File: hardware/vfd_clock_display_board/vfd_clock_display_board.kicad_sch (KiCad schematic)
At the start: 89 parts, among them J1 Conn_01x12_Pin, Q1 2N3906, Q1 MMDT5551, Q11 2N3906, Q12 2N3906, Q13 2N3906, Q14 2N3906, Q15 2N3906, Q16 2N3906, Q18 2N3906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

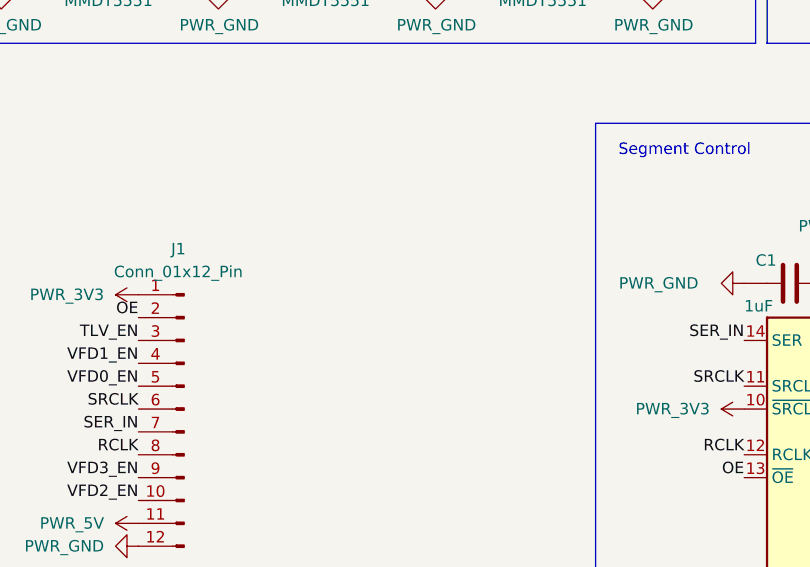
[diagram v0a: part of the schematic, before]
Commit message: Add PCF version of main board, add test pads to display board
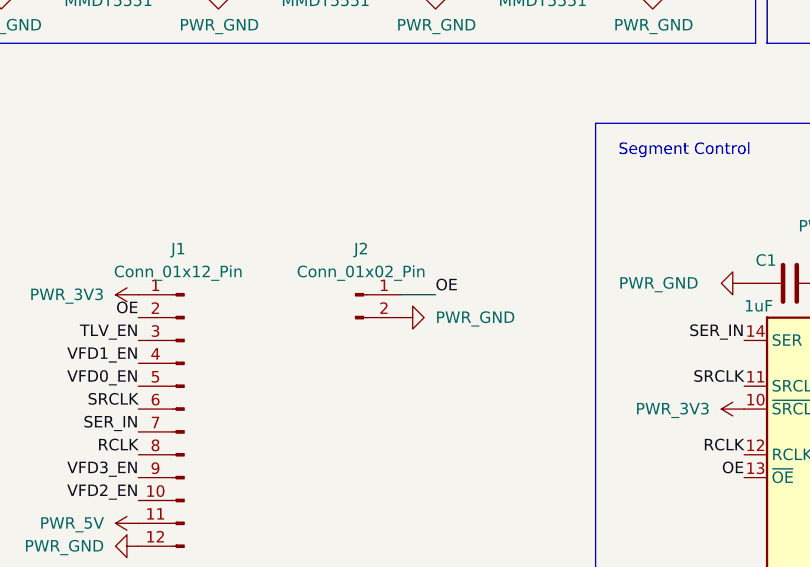
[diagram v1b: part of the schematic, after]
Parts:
- added J2: Conn_01x02_Pin, Connector_PinHeader_2.54mm:PinHeader_1x02_P2.54mm_Vertical, symbol Connector:Conn_01x02_Pin
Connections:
- net OE: now also J2.1 (Pin_1)
- net PWR_GND: now also J2.2 (Pin_2)
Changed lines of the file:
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@@
     (stroke (width 0) (type default))
   )
+  (wire (pts (xy 86.36 147.32) (xy 82.55 147.32))
+    (stroke (width 0) (type default))
+  )
   (wire (pts (xy 110.49 113.03) (xy 110.49 111.76))
     (stroke (width 0) (type default))
@@
     (effects (font (size 1.27 1.27)) (justify right bottom))
   )
-  (label "OE" (at 120.65 167.64 180) (fields_autoplaced)
-    (effects (font (size 1.27 1.27)) (justify right bottom))
-  )
   (label "0QE" (at 161.29 165.1 0) (fields_autoplaced)
     (effects (font (size 1.27 1.27)) (justify left bottom))
@@
     (effects (font (size 1.27 1.27)) (justify right bottom))
   )
+  (label "OE" (at 120.65 167.64 180) (fields_autoplaced)
+    (effects (font (size 1.27 1.27)) (justify right bottom))
+  )
   (label "VFD_C" (at 248.92 36.83 180) (fields_autoplaced)
     (effects (font (size 1.27 1.27)) (justify right bottom))
@@
     (effects (font (size 1.27 1.27)) (justify left bottom))
   )
+  (label "OE" (at 86.36 147.32 0) (fields_autoplaced)
+    (effects (font (size 1.27 1.27)) (justify left bottom))
+  )
   (label "RCLK" (at 120.65 165.1 180) (fields_autoplaced)
     (effects (font (size 1.27 1.27)) (justify right bottom))
@@
     )
   )
+  (symbol (lib_id "Fab:PWR_GND") (at 82.55 149.86 90) (mirror x) (unit 1)
+    (in_bom yes) (on_board yes) (dnp no)
+    (property "Reference" "#PWR013" (at 88.9 149.86 0)
+      (effects (font (size 1.27 1.27)) hide)
+    )
+    (property "Value" "PWR_GND" (at 86.36 149.86 90)
+      (effects (font (size 1.27 1.27)) (justify right))
+    )
+    (property "Footprint" "" (at 82.55 149.86 0)
+      (effects (font (size 1.27 1.27)) hide)
+    )
+    (property "Datasheet" "" (at 82.55 149.86 0)
+      (effects (font (size 1.27 1.27)) hide)
+    )
+    (pin "1")
+    (instances
+      (project "vfd_clock"
+        (path "/3f20cdec-fa58-4248-b6f0-db3d00e652de"
+          (reference "#PWR013") (unit 1)
+        )
+        (path "/3f20cdec-fa58-4248-b6f0-db3d00e652de/d5d05427-319c-448b-a7a3-a42b084031d1"
+          (reference "#PWR09") (unit 1)
+        )
+      )
+      (project "vfd_clock_display_board"
+        (path "/a1603893-10f9-4f34-a9ac-0449eba2410e"
+          (reference "#PWR029") (unit 1)
+        )
+      )
+      (project "vfd_pcb"
+        (path "/cb259c9d-741a-44bb-804a-c4b92b1250f0"
+          (reference "#PWR012") (unit 1)
+        )
+      )
+    )
+  )
   (symbol (lib_id "Transistor_BJT:MMDT5551") (at 100.33 106.68 0) (unit 2)
     (in_bom yes) (on_board yes) (dnp no)
@@
         )
       )
+    )
+  )
+  (symbol (lib_id "Connector:Conn_01x02_Pin") (at 77.47 147.32 0) (unit 1)
+    (in_bom yes) (on_board yes) (dnp no) (fields_autoplaced)
+    (property "Reference" "J2" (at 78.105 142.24 0)
+      (effects (font (size 1.27 1.27)))
+    )
+    (property "Value" "Conn_01x02_Pin" (at 78.105 144.78 0)
+      (effects (font (size 1.27 1.27)))
+    )
+    (property "Footprint" "Connector_PinHeader_2.54mm:PinHeader_1x02_P2.54mm_Vertical" (at 77.47 147.32 0)
+      (effects (font (size 1.27 1.27)) hide)
+    )
+    (property "Datasheet" "~" (at 77.47 147.32 0)
+      (effects (font (size 1.27 1.27)) hide)
+    )
+    (pin "1")
+    (pin "2")
+    (instances
+      (project "vfd_clock_display_board"
+        (path "/a1603893-10f9-4f34-a9ac-0449eba2410e"
+          (reference "J2") (unit 1)
+        )
+      )

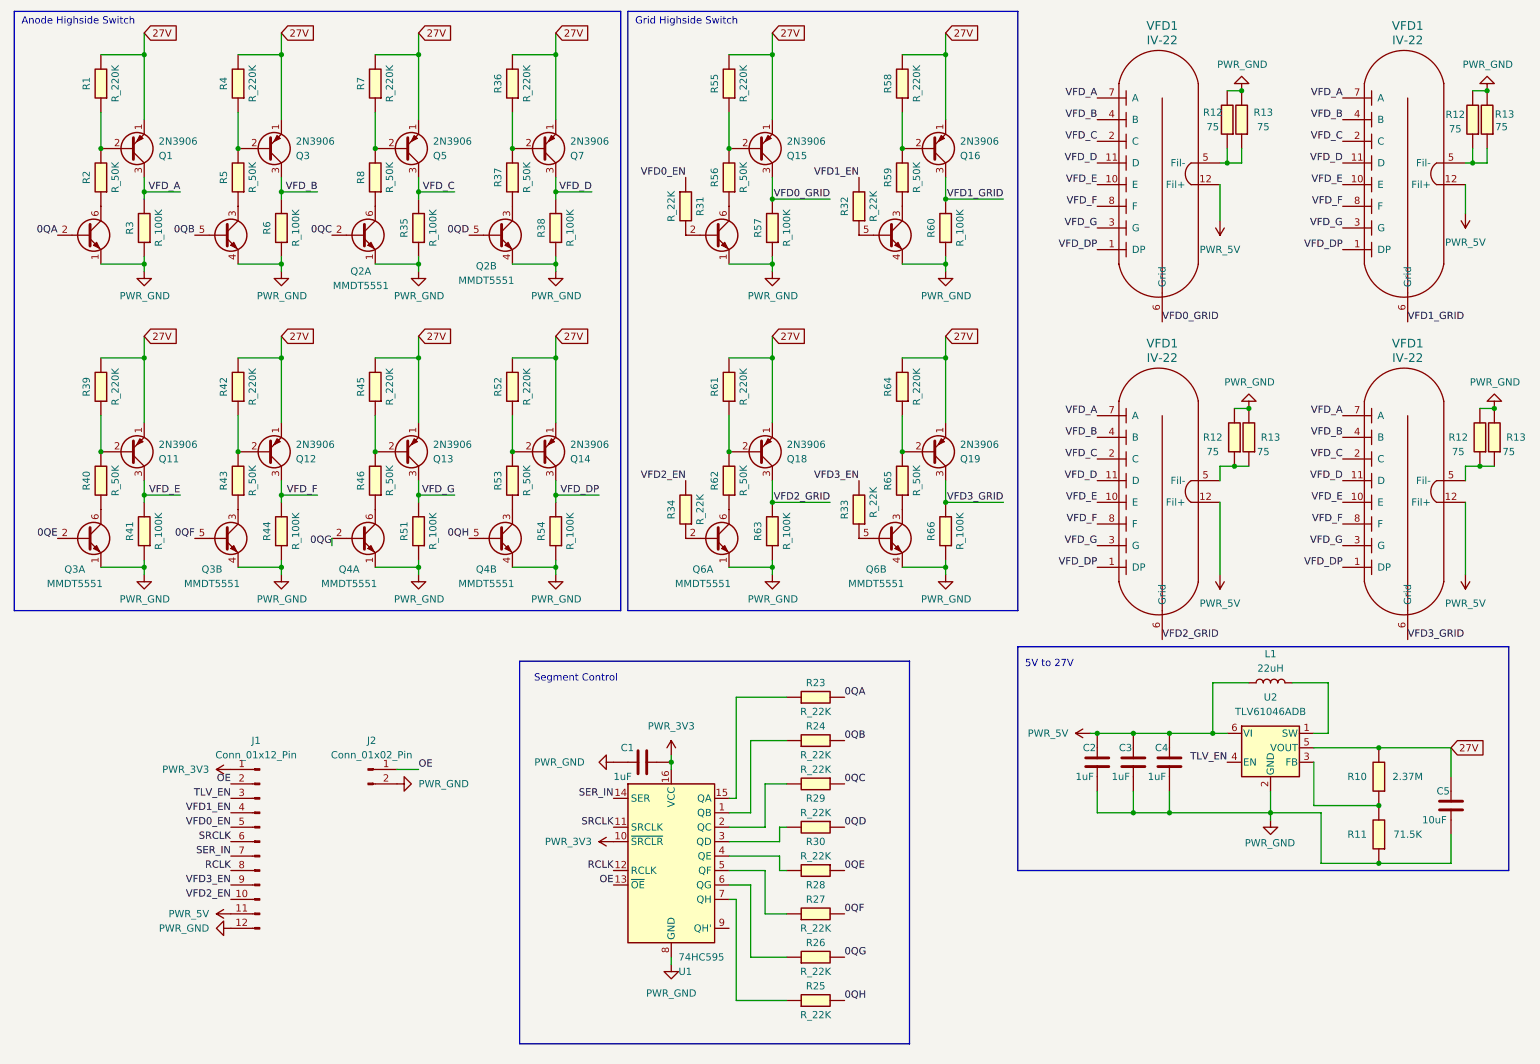
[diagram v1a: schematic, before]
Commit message: Somekind of hardware change, fix spi transaction
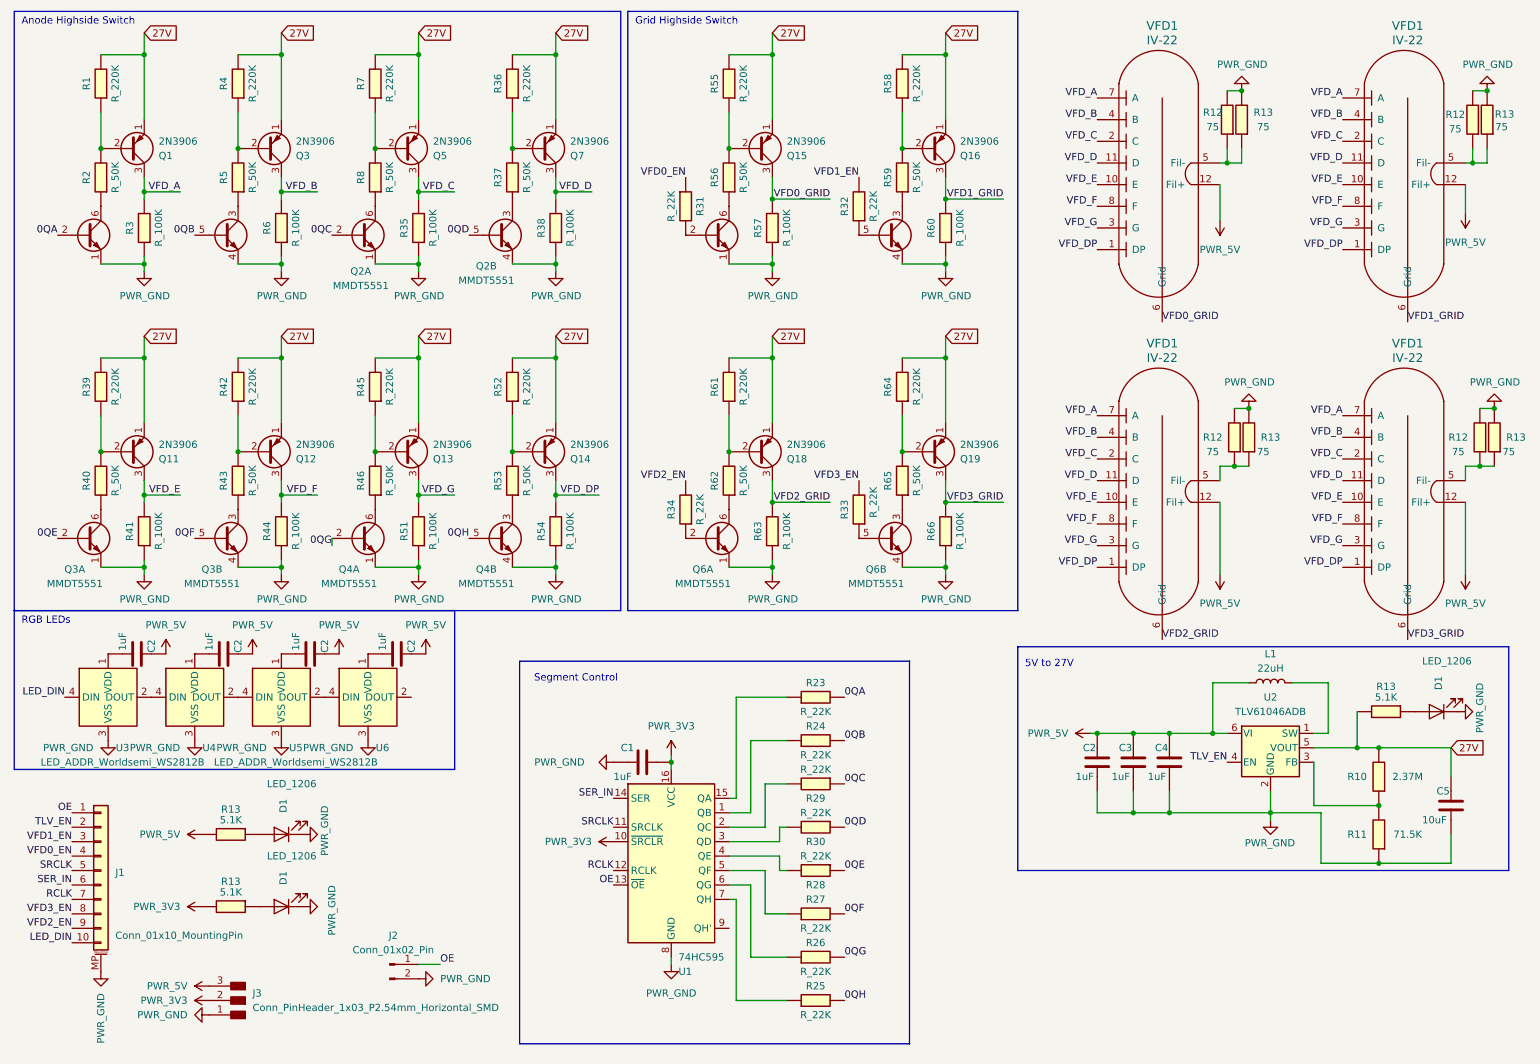
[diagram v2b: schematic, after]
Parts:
- removed J1: Conn_01x12_Pin, Connector_PinSocket_2.54mm:PinSocket_1x12_P2.54mm_Vertical, symbol Connector:Conn_01x12_Pin
- added C2 (x4): 1uF, Fab:C_1206, symbol Fab:C_1206
- added D1 (x3): LED_1206, fab:LED_1206, symbol Fab:LED_1206
- added J1: Conn_01x10_MountingPin, Connector_FFC-FPC:Molex_200528-0100_1x10-1MP_P1.00mm_Horizontal, symbol Connector_Generic_MountingPin:Conn_01x10_MountingPin
- added J3: Conn_PinHeader_1x03_P2.54mm_Horizontal_SMD, fab:PinHeader_1x03_P2.54mm_Horizontal_SMD, symbol Fab:Conn_PinHeader_1x03_P2.54mm_Horizontal_SMD
- added R13 (x3): 5.1K, Fab:R_1206, symbol Fab:R_1206
- added U3, U4, U5, U6: LED_ADDR_Worldsemi_WS2812B, Fab:LED_RGB_CreeLED_CLV1A-FKB, symbol Fab:LED_ADDR_Worldsemi_WS2812B
- L1: footprint Fab:L_1210 -> Inductor_SMD:L_Changjiang_FNR6045S
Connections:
- net 27V: now also R13.1
- net OE: now also J1.1 (Pin_1)
- net PWR_3V3: now also J3.2 (Pin_2), R13.1
- net PWR_5V: now also C2.1, C2.1, C2.1, C2.1, J3.3 (Pin_3), R13.1
- net PWR_GND: now also D1.1 (K), D1.1 (K), D1.1 (K), J1.MP (MountPin), J3.1 (Pin_1), U3.3 (VSS), U4.3 (VSS), U5.3 (VSS), U6.3 (VSS)
- net RCLK: now also J1.7 (Pin_7)
- net SER_IN: now also J1.6 (Pin_6)
- net SRCLK: now also J1.5 (Pin_5)
- net TLV_EN: now also J1.2 (Pin_2)
- net VFD0_EN: now also J1.4 (Pin_4)
- net VFD1_EN: now also J1.3 (Pin_3)
- net VFD2_EN: now also J1.9 (Pin_9)
- net VFD3_EN: now also J1.8 (Pin_8)
- new net: C2.2, U4.1 (VDD)
- new net: U4.2 (DOUT), U5.4 (DIN)
- new net: U3.2 (DOUT), U4.4 (DIN)
- new net: D1.2 (A), R13.2 (x3)
- new net: C2.2, U5.1 (VDD)
- new net: C2.2, U3.1 (VDD)
- new net: U5.2 (DOUT), U6.4 (DIN)
- new net: C2.2, U6.1 (VDD)
- new net LED_DIN: J1.10 (Pin_10), U3.4 (DIN)
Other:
- note added: "RGB LEDs"
- moved on the sheet: J2

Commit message: I forgor
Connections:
- net LED_DIN: now also J1.1 (Pin_1); no longer J1.10 (Pin_10)
- net OE: now also J1.9 (Pin_9); no longer J1.1 (Pin_1)
- net PWR_5V: now also U3.1 (VDD), U4.1 (VDD), U5.1 (VDD), U6.1 (VDD)
- net PWR_GND: now also C2.2, C2.2, C2.2, C2.2
- net RCLK: now also J1.8 (Pin_8); no longer J1.7 (Pin_7)
- net SER_IN: now also J1.10 (Pin_10); no longer J1.6 (Pin_6)
- net SRCLK: now also J1.7 (Pin_7); no longer J1.5 (Pin_5)
- net VFD0_EN: now also J1.6 (Pin_6); no longer J1.4 (Pin_4)
- net VFD1_EN: now also J1.5 (Pin_5); no longer J1.3 (Pin_3)
- net VFD2_EN: now also J1.4 (Pin_4); no longer J1.9 (Pin_9)
- net VFD3_EN: now also J1.3 (Pin_3); no longer J1.8 (Pin_8)
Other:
- moved on the sheet: C2
